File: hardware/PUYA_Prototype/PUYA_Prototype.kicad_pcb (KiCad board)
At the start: 2 copper layers, 20.1 x 31.8 mm, 11 parts, among them J1 SWD, J2 L_Terminal, J3 R_Terminal, U1 PY32F002AA15M6TU, U2 AP2112K-3.3TRG1

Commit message: Board finished plus gerbers plus BOM
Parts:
- added kibuzzard-646D3A66: G***, kibuzzard-646D3A66, F.Cu at (114.0, 69.6)
- added kibuzzard-646D3B19: G***, kibuzzard-646D3B19, F.Cu at (114.0, 66.8)
- added kibuzzard-646D3B4A: G***, kibuzzard-646D3B4A, F.Cu at (114.0, 64.3)
- added kibuzzard-646D3BD4: G***, kibuzzard-646D3BD4, F.Cu at (114.0, 61.7)
- added kibuzzard-646D3C07: G***, kibuzzard-646D3C07, F.Cu at (124.7, 61.7)
- added kibuzzard-646D3C24: G***, kibuzzard-646D3C24, F.Cu at (124.7, 64.3)
- added kibuzzard-646D3C34: G***, kibuzzard-646D3C34, F.Cu at (124.7, 66.8)
- added kibuzzard-646D3C54: G***, kibuzzard-646D3C54, F.Cu at (124.7, 69.6)
- added kibuzzard-646D3CA0: G***, kibuzzard-646D3CA0, F.Cu at (111.5, 87.4)
- added kibuzzard-646D3CAB: G***, kibuzzard-646D3CAB, F.Cu at (114.0, 87.4)
- added kibuzzard-646D3CBC: G***, kibuzzard-646D3CBC, F.Cu at (116.6, 87.4)
- added kibuzzard-646D3CFD: G***, kibuzzard-646D3CFD, F.Cu at (119.4, 87.4)
- moved J1 8.90 mm to (119.1, 89.7)
- moved D1 3.67 mm to (123.2, 88.1)
- moved R1 3.66 mm to (123.2, 85.6)
- moved C2 0.73 mm to (122.7, 62.0)
- moved C1 0.28 mm to (115.8, 62.2)
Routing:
- net GND: track 103.9 -> 10.8 mm, vias 2 -> 1
- net /SWDIO: track 7.12 -> 16.2 mm
- net /SWCLK: track 6.11 -> 15.2 mm
- net /NRST: track 33.4 -> 41.5 mm, vias 0 -> 1
- net +3.3V: track 94.9 -> 89.5 mm, vias 0 -> 2
- net /PA5: track 10.9 -> 11.8 mm
- added copper zone on B.Cu, net GND
- added copper zone on F.Cu, net GND
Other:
- board size 20.1 x 31.8 mm -> 19.3 x 31.8 mm
- board text removed: "3.3V"
- board text removed: "5V"
- board text removed: "CLK"
- board text removed: "DIO"
- board text removed: "GND"
- board text removed: "PA1"
- board text removed: "PA5"
- board text removed: "PA6"
- board text removed: "PA7"
- board text removed: "PF0"
- board text removed: "RST"

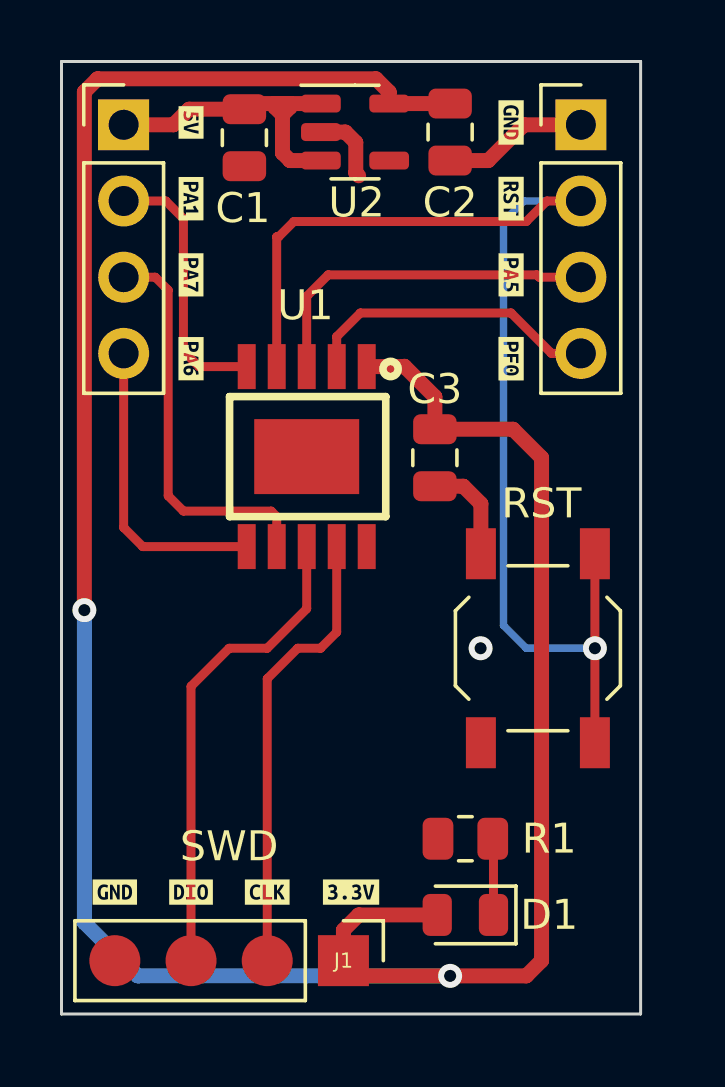
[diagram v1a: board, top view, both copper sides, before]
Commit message: Board tracks corrected
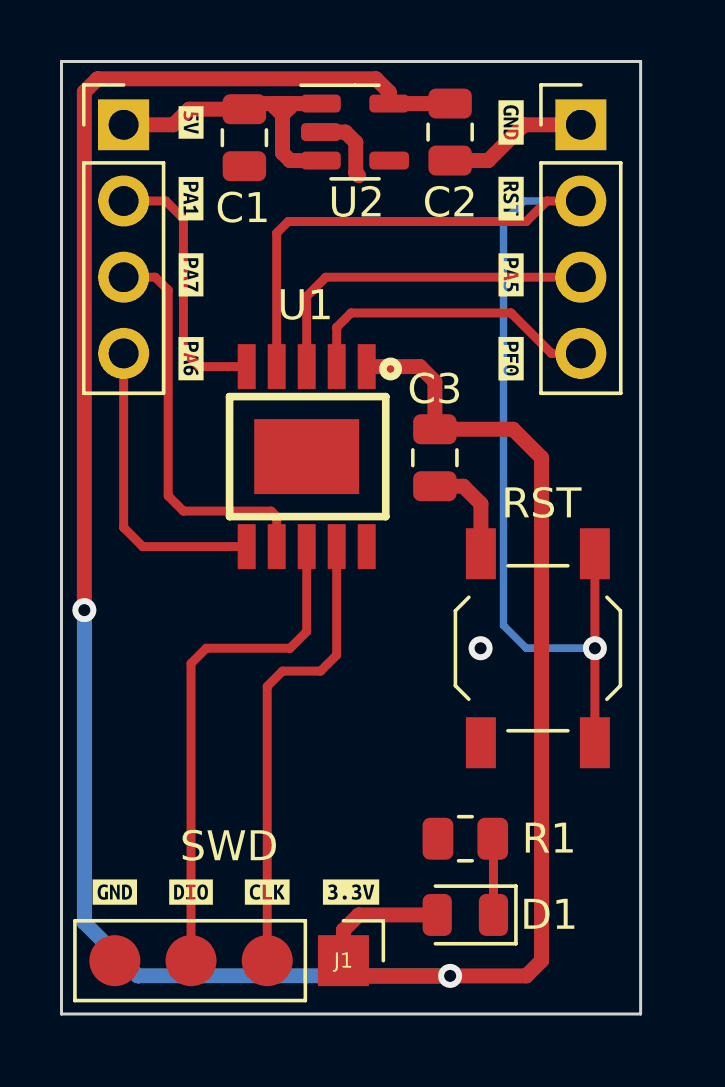
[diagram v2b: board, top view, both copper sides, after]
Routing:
- net /SWDIO: track 16.2 -> 17.1 mm

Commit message: fix traces and add EC symbols
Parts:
- added G***: LOGO, Aesthetics:electronic_cats_logo_8x6, F.Cu at (115.9, 81.1)
- added REF**: OSHW-Logo_5.7x6mm_SilkScreen, Symbol:OSHW-Logo_5.7x6mm_SilkScreen, B.Cu at (119.0, 67.1)
- renumbered D1 to ON, RST to SW1
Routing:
- net +3.3V: track 89.8 -> 48.7 mm
- net /NRST: track 41.6 -> 40.4 mm
- net GND: vias 1 -> 4
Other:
- board text added: "Dev Board PY32F"
- board text added: "v1.0"

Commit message: add pull-up resistor to NRST "DNP"
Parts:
- added R2: 10K, Resistor_SMD:R_0805_2012Metric, F.Cu at (127.5, 73.3)
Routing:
- net +3.3V: track 48.7 -> 53.7 mm
- net /NRST: track 40.4 -> 42.3 mm
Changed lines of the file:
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@@
     (property "manf#" "")
     (attr smd)
-    (fp_text reference "SW1" (at 4.826 0.122) (layer "F.SilkS")
+    (fp_text reference "SW1" (at -0.002 -3.588 90) (layer "F.SilkS")
         (effects (font (size 1 1) (thickness 0.15)))
     )
@@
     )
   )
+  (footprint "Resistor_SMD:R_0805_2012Metric" (layer "F.Cu")
+    (at 127.51 73.27 90)
+    (descr "Resistor SMD 0805 (2012 Metric), square (rectangular) end terminal, IPC_7351 nominal, (Body size source: IPC-SM-782 page 72, https://www.pcb-3d.com/wordpress/wp-content/uploads/ipc-sm-782a_amendment_1_and_2.pdf), generated with kicad-footprint-generator")
+    (tags "resistor")
+    (property "LCSC#" "C99198")
+    (property "Sheetfile" "PUYA_Prototype.kicad_sch")
+    (property "Sheetname" "")
+    (property "dnp" "")
+    (property "ki_description" "Resistor, small symbol")
+    (property "ki_keywords" "R resistor")
+    (property "manf#" "")
+    (attr smd)
+    (fp_text reference "R2" (at 0 -1.65 90) (layer "F.SilkS")
+        (effects (font (size 1 1) (thickness 0.15)))
+    )
+    (fp_text value "10K" (at 0 1.65 90) (layer "F.Fab")
+        (effects (font (size 1 1) (thickness 0.15)))
+    )
+    (fp_text user "${REFERENCE}" (at 0 0 90) (layer "F.Fab")
+        (effects (font (size 0.5 0.5) (thickness 0.08)))
+    )
+    (fp_line (start -0.227064 -0.735) (end 0.227064 -0.735)
+      (stroke (width 0.12) (type solid)) (layer "F.SilkS"))
+    (fp_line (start -0.227064 0.735) (end 0.227064 0.735)
+      (stroke (width 0.12) (type solid)) (layer "F.SilkS"))
+    (fp_line (start -1.68 -0.95) (end 1.68 -0.95)
+      (stroke (width 0.05) (type solid)) (layer "F.CrtYd"))
+    (fp_line (start -1.68 0.95) (end -1.68 -0.95)
+      (stroke (width 0.05) (type solid)) (layer "F.CrtYd"))
+    (fp_line (start 1.68 -0.95) (end 1.68 0.95)
+      (stroke (width 0.05) (type solid)) (layer "F.CrtYd"))
+    (fp_line (start 1.68 0.95) (end -1.68 0.95)
+      (stroke (width 0.05) (type solid)) (layer "F.CrtYd"))
+    (fp_line (start -1 -0.625) (end 1 -0.625)
+      (stroke (width 0.1) (type solid)) (layer "F.Fab"))
+    (fp_line (start -1 0.625) (end -1 -0.625)
+      (stroke (width 0.1) (type solid)) (layer "F.Fab"))
+    (fp_line (start 1 -0.625) (end 1 0.625)
+      (stroke (width 0.1) (type solid)) (layer "F.Fab"))
+    (fp_line (start 1 0.625) (end -1 0.625)
+      (stroke (width 0.1) (type solid)) (layer "F.Fab"))
+    (pad "1" smd roundrect (at -0.9125 0 90) (size 1.025 1.4) (layers "F.Cu" "F.Paste" "F.Mask") (roundrect_rratio 0.243902)
+      (net 7 "/NRST") (pintype "passive"))
+    (pad "2" smd roundrect (at 0.9125 0 90) (size 1.025 1.4) (layers "F.Cu" "F.Paste" "F.Mask") (roundrect_rratio 0.243902)
+      (net 3 "+3.3V") (pintype "passive"))
+    (model "${KICAD6_3DMODEL_DIR}/Resistor_SMD.3dshapes/R_0805_2012Metric.wrl"
+      (offset (xyz 0 0 0))
+      (scale (xyz 1 1 1))
+      (rotate (xyz 0 0 0))
+    )
+  )
   (footprint "kibuzzard-646D3CA0" (layer "F.Cu")
     (at 111.506 87.376)
@@
   (via (at 112.22 85.03) (size 0.8) (drill 0.4) (layers "F.Cu" "B.Cu") (free) (net 2))
   (via (at 115.38 84.81) (size 0.8) (drill 0.4) (layers "F.Cu" "B.Cu") (free) (net 2))
-  (segment (start 122.174 71.948) (end 124.09 71.948) (width 0.5) (layer "F.Cu") (net 3))
-  (segment (start 119.901998 69.860006) (end 121.676008 69.860006) (width 0.5) (layer "F.Cu") (net 3))
+  (segment (start 125.73 89.24) (end 125.73 72.87) (width 0.5) (layer "F.Cu") (net 3))
+  (segment (start 124.04 70.9) (end 124.07 70.93) (width 0.5) (layer "F.Cu") (net 3))
   (segment (start 121.84 89.63) (end 122.31 89.63) (width 0.5) (layer "F.Cu") (net 3))
-  (segment (start 125.338 71.948) (end 124.09 71.948) (width 0.5) (layer "F.Cu") (net 3))
+  (segment (start 125.73 72.08) (end 125.73 71.9) (width 0.5) (layer "F.Cu") (net 3))
+  (segment (start 126.18 72.38) (end 125.73 72.83) (width 0.5) (layer "F.Cu") (net 3))
   (segment (start 122.682 61.092) (end 122.804 60.97) (width 0.5) (layer "F.Cu") (net 3))
-  (segment (start 125.73 72.34) (end 125.338 71.948) (width 0.5) (layer "F.Cu") (net 3))
+  (segment (start 122.86 70.9) (end 122.534 70.9) (width 0.5) (layer "F.Cu") (net 3))
+  (segment (start 126.18 72.38) (end 126.18 72.35) (width 0.5) (layer "F.Cu") (net 3))
+  (segment (start 125.73 71.25) (end 125.41 70.93) (width 0.5) (layer "F.Cu") (net 3))
+  (segment (start 125.34 89.63) (end 125.73 89.24) (width 0.5) (layer "F.Cu") (net 3))
+  (segment (start 122.86 70.9) (end 124.04 70.9) (width 0.5) (layer "F.Cu") (net 3))
+  (segment (start 125.41 70.93) (end 124.07 70.93) (width 0.5) (layer "F.Cu") (net 3))
+  (segment (start 122.594 70.9) (end 122.174 71.32) (width 0.5) (layer "F.Cu") (net 3))
+  (segment (start 122.534 70.9) (end 122.174 70.54) (width 0.5) (layer "F.Cu") (net 3))
   (segment (start 122.2525 88.97) (end 122.2525 89.2175) (width 0.5) (layer "F.Cu") (net 3))
+  (segment (start 121.75 69.860006) (end 119.901998 69.860006) (width 0.5) (layer "F.Cu") (net 3))
+  (segment (start 127.4875 72.38) (end 127.51 72.3575) (width 0.5) (layer "F.Cu") (net 3))
+  (segment (start 122.86 70.9) (end 122.594 70.9) (width 0.5) (layer "F.Cu") (net 3))
   (segment (start 122.2525 88.97) (end 122.2525 89.1325) (width 0.5) (layer "F.Cu") (net 3))
+  (segment (start 125.73 71.9) (end 125.73 71.25) (width 0.5) (layer "F.Cu") (net 3))
   (segment (start 122.75 89.63) (end 125.34 89.63) (width 0.5) (layer "F.Cu") (net 3))
-  (segment (start 125.73 89.24) (end 125.73 72.34) (width 0.5) (layer "F.Cu") (net 3))
-  (segment (start 122.174 70.358) (end 121.676008 69.860006) (width 0.5) (layer "F.Cu") (net 3))
+  (segment (start 126.18 72.38) (end 126.03 72.38) (width 0.5) (layer "F.Cu") (net 3))
+  (segment (start 125.73 72.38) (end 125.73 72.08) (width 0.5) (layer "F.Cu") (net 3))
+  (segment (start 122.174 70.54) (end 122.174 70.284006) (width 0.5) (layer "F.Cu") (net 3))
+  (segment (start 122.174 71.32) (end 122.174 70.9) (width 0.5) (layer "F.Cu") (net 3))
+  (segment (start 125.73 72.83) (end 125.73 72.87) (width 0.5) (layer "F.Cu") (net 3))
   (segment (start 122.682 61.092) (end 120.65 61.092) (width 0.5) (layer "F.Cu") (net 3))
-  (segment (start 122.174 71.948) (end 122.174 70.358) (width 0.5) (layer "F.Cu") (net 3))
-  (segment (start 125.34 89.63) (end 125.73 89.24) (width 0.5) (layer "F.Cu") (net 3))
+  (segment (start 122.174 71.948) (end 122.174 71.32) (width 0.5) (layer "F.Cu") (net 3))
+  (segment (start 125.73 72.87) (end 125.73 72.38) (width 0.5) (layer "F.Cu") (net 3))
+  (segment (start 126.18 72.35) (end 125.73 71.9) (width 0.5) (layer "F.Cu") (net 3))
+  (segment (start 125.73 72.38) (end 126.18 72.38) (width 0.5) (layer "F.Cu") (net 3))
+  (segment (start 122.174 70.9) (end 122.174 70.54) (width 0.5) (layer "F.Cu") (net 3))
+  (segment (start 126.18 72.38) (end 127.4875 72.38) (width 0.5) (layer "F.Cu") (net 3))
+  (segment (start 122.174 70.9) (end 122.86 70.9) (width 0.5) (layer "F.Cu") (net 3))
   (segment (start 122.804 60.97) (end 124.12 60.97) (width 0.5) (layer "F.Cu") (net 3))
   (segment (start 119.126 89.63) (end 121.84 89.63) (width 0.5) (layer "F.Cu") (net 3))
@@
   (segment (start 122.2525 89.2175) (end 121.84 89.63) (width 0.5) (layer "F.Cu") (net 3))
   (segment (start 122.31 89.63) (end 122.75 89.63) (width 0.5) (layer "F.Cu") (net 3))
+  (segment (start 122.174 70.284006) (end 121.75 69.860006) (width 0.5) (layer "F.Cu") (net 3))
   (segment (start 122.31 88.1955) (end 122.2525 88.138) (width 0.5) (layer "F.Cu") (net 3))
-  (segment (start 122.24 71.882) (end 122.174 71.948) (width 0.5) (layer "F.Cu") (net 3))
   (segment (start 122.2525 88.138) (end 122.2525 88.97) (width 0.5) (layer "F.Cu") (net 3))
   (via (at 124.12 60.97) (size 0.8) (drill 0.4) (layers "F.Cu" "B.Cu") (net 3))
-  (via (at 124.09 71.948) (size 0.8) (drill 0.4) (layers "F.Cu" "B.Cu") (net 3))
-  (segment (start 124.07 71.928) (end 124.09 71.948) (width 0.5) (layer "B.Cu") (net 3))
-  (segment (start 124.07 61.02) (end 124.07 71.928) (width 0.5) (layer "B.Cu") (net 3))
+  (via (at 124.07 70.93) (size 0.8) (drill 0.4) (layers "F.Cu" "B.Cu") (net 3))
+  (segment (start 124.07 61.02) (end 124.07 70.93) (width 0.5) (layer "B.Cu") (net 3))
   (segment (start 124.12 60.97) (end 124.07 61.02) (width 0.5) (layer "B.Cu") (net 3))
   (segment (start 124.1025 85.598) (end 124.1275 85.623) (width 0.3) (layer "F.Cu") (net 4))
@@
   (segment (start 125.222 65.024) (end 125.906 64.34) (width 0.3) (layer "F.Cu") (net 7))
   (segment (start 126.46 64.34) (end 127.04 64.34) (width 0.3) (layer "F.Cu") (net 7))
+  (segment (start 127.508 76.098) (end 127.508 74.1845) (width 0.3) (layer "F.Cu") (net 7))
   (segment (start 117.2845 65.024) (end 125.222 65.024) (width 0.3) (layer "F.Cu") (net 7))
+  (segment (start 127.508 74.1845) (end 127.51 74.1825) (width 0.3) (layer "F.Cu") (net 7))
   (segment (start 127.508 76.098) (end 127.508 82.398) (width 0.3) (layer "F.Cu") (net 7))
   (segment (start 116.902004 69.860006) (end 116.902004 65.406496) (width 0.3) (layer "F.Cu") (net 7))

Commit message: add library.pretty
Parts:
- U1: footprint Libraries:ESSOP10-EP -> PY32F002:PY32F002AA15M
- renumbered ON to D1
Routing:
- net GND: vias 4 -> 14
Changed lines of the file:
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@@
     (property "manf#" "")
     (attr smd)
-    (fp_text reference "ON" (at -2.794 0 180) (layer "F.SilkS")
+    (fp_text reference "D1" (at -2.794 0 180) (layer "F.SilkS")
         (effects (font (size 1 1) (thickness 0.15)))
     )
@@
       (stroke (width 0) (type solid)) (fill solid) (layer "F.SilkS"))
   )
-  (footprint "Libraries:ESSOP10-EP" (layer "F.Cu")
+  (footprint "PY32F002:PY32F002AA15M" (layer "F.Cu")
     (at 117.902002 72.859873 -90)
     (property "LCSC#" "C5292058")
@@
     (property "manf#" "")
     (attr through_hole)
-    (fp_text reference "U1" (at -5.041873 0.046002) (layer "F.SilkS")
+    (fp_text reference "U1" (at -1.119873 3.382002 90) (layer "F.SilkS")
         (effects (font (size 1 1) (thickness 0.15)))
     )
-    (fp_text value "PY32F002AA15M6TU" (at 0 0 90) (layer "F.Fab")
+    (fp_text value "PY32F002AA15M6TU" (at 0 3.5 90) (layer "F.Fab")
         (effects (font (size 1 1) (thickness 0.15)))
     )
@@
   (segment (start 123.708 79.258) (end 123.698 79.248) (width 0.5) (layer "F.Cu") (net 2))
   (segment (start 123.952 62.992) (end 125.144 61.8) (width 0.5) (layer "F.Cu") (net 2))
+  (via (at 128 87.5) (size 0.8) (drill 0.4) (layers "F.Cu" "B.Cu") (free) (net 2))
+  (via (at 123.5 91) (size 0.8) (drill 0.4) (layers "F.Cu" "B.Cu") (free) (net 2))
+  (via (at 110.5 71.5) (size 0.8) (drill 0.4) (layers "F.Cu" "B.Cu") (free) (net 2))
+  (via (at 110.5 77.5) (size 0.8) (drill 0.4) (layers "F.Cu" "B.Cu") (free) (net 2))
   (via (at 123.698 79.248) (size 0.8) (drill 0.4) (layers "F.Cu" "B.Cu") (free) (net 2))
+  (via (at 115.45 67.21) (size 0.8) (drill 0.4) (layers "F.Cu" "B.Cu") (free) (net 2))
+  (via (at 114.59 73.66) (size 0.8) (drill 0.4) (layers "F.Cu" "B.Cu") (free) (net 2))
   (via (at 118.61 84.87) (size 0.8) (drill 0.4) (layers "F.Cu" "B.Cu") (free) (net 2))
+  (via (at 110.5 74.5) (size 0.8) (drill 0.4) (layers "F.Cu" "B.Cu") (free) (net 2))
   (via (at 112.22 85.03) (size 0.8) (drill 0.4) (layers "F.Cu" "B.Cu") (free) (net 2))
+  (via (at 128 85.5) (size 0.8) (drill 0.4) (layers "F.Cu" "B.Cu") (free) (net 2))
   (via (at 115.38 84.81) (size 0.8) (drill 0.4) (layers "F.Cu" "B.Cu") (free) (net 2))
+  (via (at 128 89.5) (size 0.8) (drill 0.4) (layers "F.Cu" "B.Cu") (free) (net 2))
+  (via (at 126.5 91) (size 0.8) (drill 0.4) (layers "F.Cu" "B.Cu") (free) (net 2))
   (segment (start 125.73 89.24) (end 125.73 72.87) (width 0.5) (layer "F.Cu") (net 3))
   (segment (start 124.04 70.9) (end 124.07 70.93) (width 0.5) (layer "F.Cu") (net 3))

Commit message: fix library
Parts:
- U1: footprint PY32F002:PY32F002AA15M -> Librarie:PY32F002AA15M
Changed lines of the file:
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@@
       (stroke (width 0) (type solid)) (fill solid) (layer "F.SilkS"))
   )
-  (footprint "PY32F002:PY32F002AA15M" (layer "F.Cu")
+  (footprint "Librarie:PY32F002AA15M" (layer "F.Cu")
     (at 117.902002 72.859873 -90)
     (property "LCSC#" "C5292058")
@@
     (property "manf#" "")
     (attr through_hole)
-    (fp_text reference "U1" (at -1.119873 3.382002 90) (layer "F.SilkS")
+    (fp_text reference "U1" (at -1.359873 3.402002 -90) (layer "F.SilkS")
         (effects (font (size 1 1) (thickness 0.15)))
     )
-    (fp_text value "PY32F002AA15M6TU" (at 0 3.5 90) (layer "F.Fab")
+    (fp_text value "PY32F002AA15M6TU" (at 0 3.5 -90) (layer "F.Fab")
         (effects (font (size 1 1) (thickness 0.15)))
     )
